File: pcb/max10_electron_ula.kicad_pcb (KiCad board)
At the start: 4 copper layers, 55 x 89 mm, 86 parts

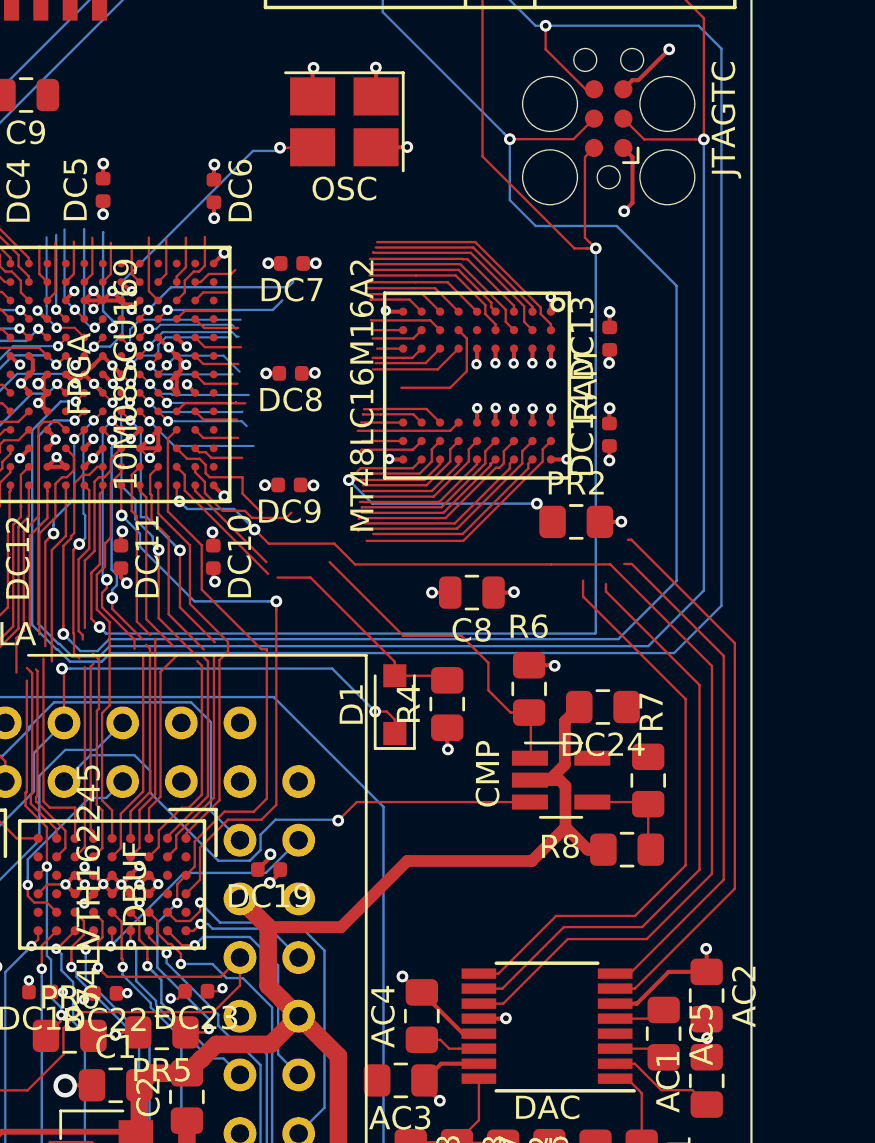
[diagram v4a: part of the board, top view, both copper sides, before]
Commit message: SDRAM wiring also looking good.  Time to verify in Quartus.
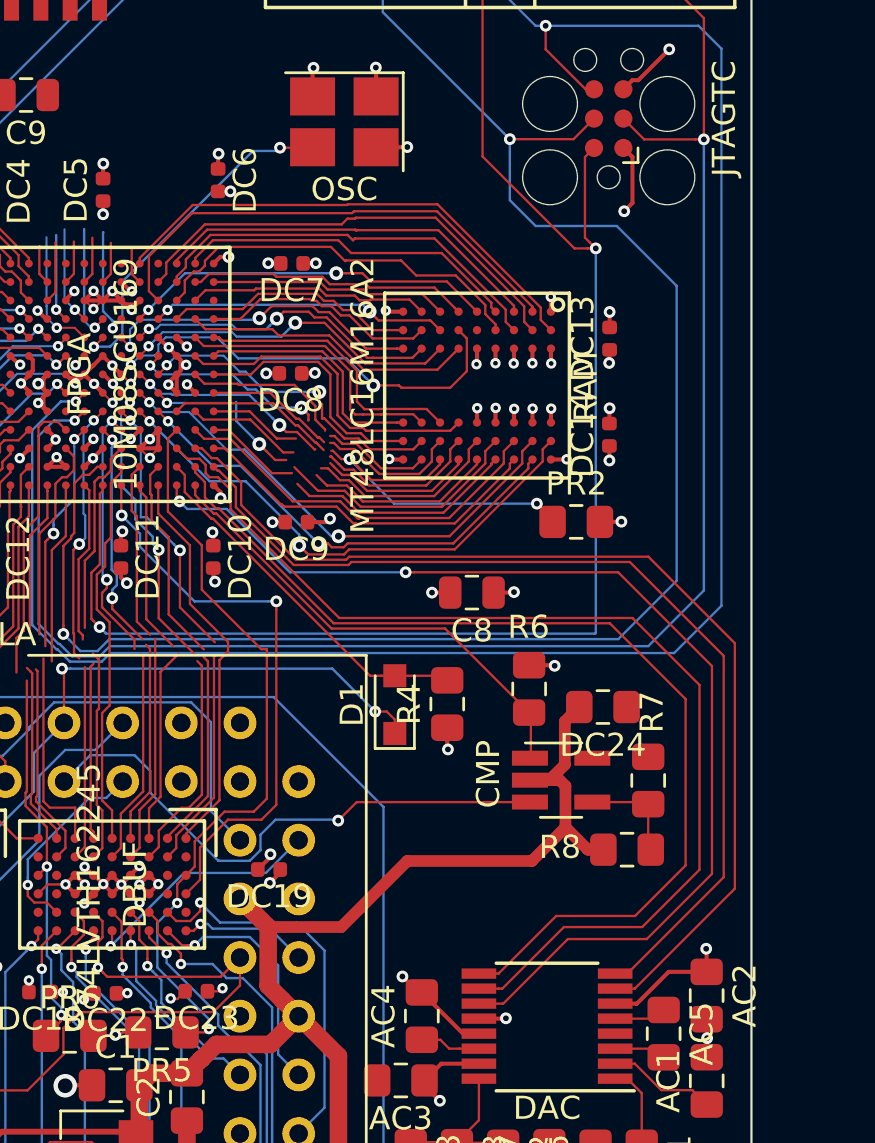
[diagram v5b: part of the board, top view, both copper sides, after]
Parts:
- moved DC9 1.64 mm to (182.5, 49.5)
- moved DC6 0.50 mm to (179.1, 34.7)
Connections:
- FPGA pad H8: sdram_BA0 -> sdram_CLK
- FPGA pad H9: sdram_A7 -> sdram_A4
- FPGA pad J10: sdram_DQ12 -> sdram_DQ8
- FPGA pad J5: sdram_DQ1 -> sdram_DQ0
- FPGA pad J6: sdram_DQ6 -> sdram_DQ2
- FPGA pad J7: sdram_nRAS -> sdram_nWE
- FPGA pad J8: sdram_CLK -> sdram_A9
- FPGA pad K10: sdram_DQ10 -> sdram_A11
- FPGA pad K5: sdram_DQ4 -> sdram_DQ1
- FPGA pad K6: sdram_nWE -> sdram_DQ6
- FPGA pad K7: sdram_A2 -> sdram_A1
- FPGA pad K8: sdram_A1 -> sdram_BA1
- FPGA pad L11: sdram_UDQM -> sdram_DQ9
- FPGA pad L13: sdram_DQ9 -> sdram_DQ12
- FPGA pad L5: sdram_LDQM -> sdram_nRAS
- FPGA pad M10: sdram_A9 -> sdram_CKE
- FPGA pad M11: sdram_A11 -> sdram_A8
- FPGA pad M12: sdram_A12 -> sdram_UDQM
- FPGA pad M13: sdram_DQ8 -> sdram_DQ10
- FPGA pad M3: dac_lrclk -> dac_dacdat
- FPGA pad M4: sdram_DQ2 -> sdram_DQ4
- FPGA pad M5: sdram_DQ5 -> sdram_DQ7
- FPGA pad M7: sdram_BA1 -> sdram_A10
- FPGA pad N10: sdram_A4 -> sdram_A7
- FPGA pad N12: sdram_A8 -> sdram_A12
- FPGA pad N2: dac_dacdat -> dac_lrclk
- FPGA pad N3: sdram_DQ0 -> sdram_DQ3
- FPGA pad N4: sdram_DQ3 -> sdram_DQ5
- FPGA pad N5: sdram_DQ7 -> sdram_LDQM
- FPGA pad N7: sdram_A10 -> sdram_A2
- FPGA pad N9: sdram_CKE -> sdram_BA0
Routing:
- net dac_dacdat: track 24.1 -> 45.1 mm
- net dac_lrclk: track 24.2 -> 42.1 mm
- net dac_mclk: track 31.2 -> 47.3 mm
- net dac_bclk: track 30.7 -> 44.0 mm
- net sdram_A4: track 1.13 -> 14.3 mm, vias 0 -> 2
- net sdram_DQ0: track 10.1 -> 23.0 mm, vias 0 -> 2
- net sdram_DQ15: track 9.42 -> 21.6 mm
- net sdram_DQ8: track 5.28 -> 16.1 mm, vias 0 -> 2
- net sdram_DQ14: track 11.0 -> 21.4 mm
- net sdram_DQ9: track 6.81 -> 17.1 mm
- net sdram_DQ2: track 11.5 -> 21.6 mm, vias 0 -> 2
- net sdram_A9: track 5.08 -> 14.8 mm, vias 0 -> 2
- net sdram_DQ13: track 10.7 -> 20.1 mm
- net sdram_CLK: track 9.87 -> 18.9 mm, vias 1 -> 2
- net sdram_A3: track 1.82 -> 10.6 mm
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
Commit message: Possibly final FPGA pin assignment; PCB looking pretty good too
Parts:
- moved PR3 2.80 mm to (160.8, 32.6)
- moved PR11 2.23 mm to (164.5, 32.6), turned to 0 degrees
- moved DC4 0.61 mm to (169.1, 34.7), turned to 0 degrees
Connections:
- FPGA pad D11: sd_CMD_MOSI -> USB_P
- FPGA pad D12: USB_M -> USB_PU
- FPGA pad E10: USB_PU -> sd_CMD_MOSI
- FPGA pad E13: sd_DAT0_MISO -> USB_M
- FPGA pad F10: sd_CLK_SCK -> sd_DAT2
- FPGA pad F12: sd_DAT3_nCS -> flash_IO1
- FPGA pad F13: sd_DAT2 -> flash_nCE
- FPGA pad F9: USB_P -> sd_DAT3_nCS
- FPGA pad G10: flash_SCK -> sd_CLK_SCK
- FPGA pad G12: flash_IO0 -> flash_IO3
- FPGA pad G13: flash_nCE -> flash_IO2
- FPGA pad H10: flash_IO2 -> sd_DAT0_MISO
- FPGA pad H13: flash_IO1 -> flash_SCK
- FPGA pad H2: clk_in -> data0
- FPGA pad H4: data0 -> clk_in
- FPGA pad J12: flash_IO3 -> flash_IO0
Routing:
- net sd_DAT0_MISO: track 0.00 -> 33.5 mm, vias 0 -> 2
- net sd_DAT1: track 1.90 -> 31.4 mm, vias 0 -> 2
- net sd_DAT2: track 0.00 -> 28.7 mm, vias 0 -> 2
- net sd_DAT3_nCS: track 2.06 -> 30.5 mm, vias 0 -> 3
- net sd_CMD_MOSI: track 2.66 -> 30.4 mm, vias 0 -> 3
- net sd_CLK_SCK: track 4.25 -> 31.9 mm, vias 1 -> 2
- net flash_IO3: track 1.66 -> 21.6 mm
- net flash_IO0: track 1.84 -> 20.7 mm
- net flash_nCE: track 0.00 -> 16.0 mm
- net USB_M: track 1.70 -> 17.4 mm
- net flash_SCK: track 5.08 -> 20.1 mm, vias 1 -> 0
- net flash_IO1: track 0.00 -> 13.2 mm
- net USB_PU: track 3.82 -> 16.6 mm, vias 1 -> 0
- net USB_P: track 5.47 -> 17.9 mm, vias 1 -> 0
- net 3V3: track 92.3 -> 101.6 mm, vias 71 -> 76
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- added copper zone on In2.Cu, net 3V3
- added copper zone on In1.Cu, net GND
- removed copper zone on In1.Cu, net 3V3
- removed copper zone on In2.Cu, net GND
